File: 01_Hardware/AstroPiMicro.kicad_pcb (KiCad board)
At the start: 2 copper layers, 65 x 50.2 mm, 52 parts, among them J1 RPi Connector, J10 B6B-PH-K(LF)(SN), J2 USB_C_Receptacle_USB2.0, J3 C47647, J4 I2C_IMU, J5 A1002WV-S-4P, J6 B11B-PH-K-S(LF)(SN), J7 B3B-PH-K-S(LF)(SN), J8 CON_SW_B, J9 CON_JOY_B, SW1 SSSS213202, U1 LM809, U2 STM32G431KBTx, U3 MCP73831-2-OT, U4 TPS61090, U5 SKRHAAE010, Y1 X1H016000FI1H-X

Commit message: Finished BOM, PCB and ordered PCB
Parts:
- added G***: LOGO, astropi:qr, B.Cu at (106.5, 63.5)
- D1: value HSMF-C155 -> Status LED
- J10: value B6B-PH-K(LF)(SN) -> 6-pin JST PH
- J3: value C47647 -> 2-pin JST PH
- J4: value I2C_IMU -> 4-pin JST SH
- J5: value A1002WV-S-4P -> 4-pin JST SH
- J6: value B11B-PH-K-S(LF)(SN) -> 11-pin JST PH
- J7: value B3B-PH-K-S(LF)(SN) -> 3-pin JST PH
- J8: value CON_SW_B -> 3-pin JST PH
- J9: value CON_JOY_B -> 6-pin JST PH
- L1: value DR73-6R8-R -> 6.8uH; footprint astropi:DR73 -> Inductor_SMD:L_Taiyo-Yuden_NR-50xx_HandSoldering
- R9: value 2.1Meg -> 2.1M
- SW1: value SSSS213202 -> SW-ON-OFF
- U5: value SKRHAAE010 -> Joystick
- Y1: value X1H016000FI1H-X -> 16MHz
- moved L1 1.11 mm to (64.2, 67.2)
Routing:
- net /GPIO27: track 27.2 -> 26.1 mm, vias 3 -> 2
- net Net-(L1-Pad2): track 6.29 -> 7.15 mm
- net /GPIO17: track 28.7 -> 29.4 mm
- net +3V3: track 61.6 -> 62.1 mm
- net (no net): vias 16 -> 0
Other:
- outline, holes or cut-outs redrawn
- board text added: "[Geanina]"

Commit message: Started on HW version 2
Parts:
- removed the ? at (53.6, 75.5)
- removed the ? at (111.6, 75.6)
- removed G***: LOGO, astropi:qr
- removed J10: 6-pin JST PH, Connector_JST:JST_PH_B6B-PH-K_1x06_P2.00mm_Vertical
- removed J8: 3-pin JST PH, Connector_JST:JST_PH_B3B-PH-SM4-TB_1x03-1MP_P2.00mm_Vertical
- removed J9: 6-pin JST PH, Connector_JST:JST_PH_B6B-PH-SM4-TB_1x06-1MP_P2.00mm_Vertical
- removed REF** (x8): MountingHole_2.2mm_M2_ISO14580_Pad, MountingHole:MountingHole_2.2mm_M2_ISO14580_Pad
- removed Y1: 16MHz, Crystal:Crystal_SMD_Abracon_ABM3B-4Pin_5.0x3.2mm
- added ?: , RPi_Hat:RPi_Hat_Mounting_Hole, F.Cu at (53.6, 101.5)
- added ?: , RPi_Hat:RPi_Hat_Mounting_Hole, F.Cu at (111.6, 101.5)
- added C11: 100nF, Capacitor_SMD:C_0603_1608Metric, F.Cu at (102.7, 73.4)
- added C12: 100nF, Capacitor_SMD:C_0603_1608Metric, F.Cu at (98.2, 62.6)
- added C13: 47uF, Capacitor_Tantalum_SMD:CP_EIA-3528-15_AVX-H, F.Cu at (99.3, 67.4)
- added C14: 100nF, Capacitor_SMD:C_0603_1608Metric, F.Cu at (101.2, 59.5)
- added C15: 100nF, Capacitor_SMD:C_0603_1608Metric, F.Cu at (102.7, 87.1)
- added C16: 100nF, Capacitor_SMD:C_0603_1608Metric, F.Cu at (98.3, 90.4)
- added C17: 47uF, Capacitor_Tantalum_SMD:CP_EIA-3528-15_AVX-H, F.Cu at (99.6, 94.9)
- added C18: 100nF, Capacitor_SMD:C_0603_1608Metric, F.Cu at (101.1, 87.1)
- added C3: 4.7uF, Capacitor_SMD:C_0805_2012Metric, F.Cu at (67.0, 89.7)
- added D2: Orange, LED_SMD:LED_0603_1608Metric, F.Cu at (63.0, 86.2)
- added QR*****: MiniCalinGeani, astropi:MiniCalinGeani, F.Cu at (80.7, 66.9)
- added R11: 0.75, Resistor_SMD:R_0603_1608Metric, F.Cu at (99.0, 73.4)
- added R14: 0.75, Resistor_SMD:R_0603_1608Metric, F.Cu at (103.1, 80.9)
- added R15: 1k, Resistor_SMD:R_0603_1608Metric, F.Cu at (97.8, 59.5)
- added R16: 220m, Resistor_SMD:R_0603_1608Metric, F.Cu at (99.4, 59.5)
- added R17: 220m, Resistor_SMD:R_0603_1608Metric, F.Cu at (102.7, 67.3)
- added R18: 1k, Resistor_SMD:R_0603_1608Metric, F.Cu at (97.7, 87.1)
- added R19: 220m, Resistor_SMD:R_0603_1608Metric, F.Cu at (99.3, 87.1)
- added R20: 220m, Resistor_SMD:R_0603_1608Metric, F.Cu at (103.0, 94.8)
- added R21: 10k, Resistor_SMD:R_0603_1608Metric, F.Cu at (57.8, 91.0)
- added TP1: TP_VBAT, TestPoint:TestPoint_Pad_D2.0mm, F.Cu at (68.9, 75.9)
- added TP2: TP_Supply, TestPoint:TestPoint_Pad_D2.0mm, F.Cu at (73.8, 94.4)
- added TP3: TP_5V, TestPoint:TestPoint_Pad_D2.0mm, F.Cu at (87.2, 81.7)
- added TP4: TP_GND, TestPoint:TestPoint_Pad_2.5x2.5mm, F.Cu at (79.9, 103.2)
- C1: value 27pF -> 100nF; footprint Capacitor_SMD:C_0603_1608Metric_Pad1.05x0.95mm_HandSolder -> Capacitor_SMD:C_0603_1608Metric
- C10: footprint Capacitor_Tantalum_SMD:CP_EIA-7343-31_Kemet-D_Pad2.25x2.55mm_HandSolder -> Capacitor_Tantalum_SMD:CP_EIA-7343-15_Kemet-W
- C2: value 27pF -> 1uF; footprint Capacitor_SMD:C_0603_1608Metric_Pad1.05x0.95mm_HandSolder -> Capacitor_SMD:C_0805_2012Metric
- C4: value 100nF -> 10uF; footprint Capacitor_SMD:C_0603_1608Metric_Pad1.05x0.95mm_HandSolder -> Capacitor_SMD:C_0805_2012Metric
- C5: value 10uF -> 100nF; footprint Capacitor_SMD:C_0805_2012Metric -> Capacitor_SMD:C_0603_1608Metric
- C6: value 100nF -> 47uF; footprint Capacitor_SMD:C_0603_1608Metric_Pad1.05x0.95mm_HandSolder -> Capacitor_Tantalum_SMD:CP_EIA-3528-15_AVX-H
- C7: footprint Capacitor_SMD:C_0603_1608Metric_Pad1.05x0.95mm_HandSolder -> Capacitor_SMD:C_0603_1608Metric
- D1: value Status LED -> Green; footprint LED_SMD:LED_Avago_PLCC4_3.2x2.8mm_CW -> LED_SMD:LED_0603_1608Metric
- J2: value USB_C_Receptacle_USB2.0 -> SHOU_HAN_TYPE-C_6P; footprint astropi:USB_C_GCT_USB4085 -> astropi:SHOU HAN TYPE-C 6P
- J3, J4: moved to F.Cu
- J5: value 4-pin JST SH -> Stepper_Focus; footprint Connector_JST:JST_SH_BM04B-SRSS-TB_1x04-1MP_P1.00mm_Vertical -> Connector_JST:JST_XH_S4B-XH-A_1x04_P2.50mm_Horizontal
- J6: value 11-pin JST PH -> Stepper_Azimuth; footprint Connector_JST:JST_PH_B11B-PH-K_1x11_P2.00mm_Vertical -> Connector_JST:JST_XH_S4B-XH-A_1x04_P2.50mm_Horizontal
- J7: value 3-pin JST PH -> Stepper_Altitude; footprint Connector_JST:JST_PH_B3B-PH-K_1x03_P2.00mm_Vertical -> Connector_JST:JST_XH_S4B-XH-A_1x04_P2.50mm_Horizontal
- L1: value 6.8uH -> 10uH; footprint Inductor_SMD:L_Taiyo-Yuden_NR-50xx_HandSoldering -> astropi:VLS6045EX-100M
- R1: value 10k -> 1.1k; footprint Resistor_SMD:R_0603_1608Metric_Pad1.05x0.95mm_HandSolder -> Resistor_SMD:R_0603_1608Metric
- R10, R12, R13, R4, R5, R7, R8, R9: footprint Resistor_SMD:R_0603_1608Metric_Pad1.05x0.95mm_HandSolder -> Resistor_SMD:R_0603_1608Metric
- R2: value 10k -> 1k; footprint Resistor_SMD:R_0603_1608Metric_Pad1.05x0.95mm_HandSolder -> Resistor_SMD:R_0603_1608Metric
- R3: value 10k -> 1.5k; footprint Resistor_SMD:R_0603_1608Metric_Pad1.05x0.95mm_HandSolder -> Resistor_SMD:R_0603_1608Metric
- R6: value 2k -> 10k; footprint Resistor_SMD:R_0603_1608Metric_Pad1.05x0.95mm_HandSolder -> Resistor_SMD:R_0603_1608Metric
- SW1: value SW-ON-OFF -> SW_SPDT; footprint astropi:SSSS213202 -> Button_Switch_SMD:SW_SPDT_CK-JS102011SAQN
- U1: value LM809 -> BQ24074RGT; footprint Package_TO_SOT_SMD:SOT-23 -> Package_DFN_QFN:VQFN-16-1EP_3x3mm_P0.5mm_EP1.6x1.6mm_ThermalVias
- U2: value STM32G431KBTx -> TMC2300; footprint Package_QFP:LQFP-32_7x7mm_P0.8mm -> Package_DFN_QFN:QFN-20-1EP_3x3mm_P0.4mm_EP1.65x1.65mm_ThermalVias
- U3: value MCP73831-2-OT -> TMC2300; footprint Package_TO_SOT_SMD:SOT-23-5 -> Package_DFN_QFN:QFN-20-1EP_3x3mm_P0.4mm_EP1.65x1.65mm_ThermalVias
- U5: value Joystick -> TMC2300; footprint astropi:SKRHAAE010 -> Package_DFN_QFN:QFN-20-1EP_3x3mm_P0.4mm_EP1.65x1.65mm_ThermalVias
- moved R1 55.0 mm to (60.9, 93.3), turned to 90 degrees
- moved U1 52.7 mm to (63.9, 90.8), turned to 180 degrees
- moved C2 52.1 mm to (63.6, 94.0)
- moved C4 43.9 mm to (60.7, 89.8), turned to 90 degrees
- moved C5 43.2 mm to (98.2, 76.5)
- moved SW1 39.4 mm to (52.3, 91.6), turned to 270 degrees
- moved J2 38.1 mm to (64.0, 99.6), turned to 0 degrees
- moved J7 36.8 mm to (107.0, 94.6), turned to 90 degrees
- moved R3 36.1 mm to (66.8, 93.3), turned to 90 degrees
- moved U3 34.8 mm to (101.3, 63.2), turned to 90 degrees
- moved R4 33.7 mm to (63.1, 96.7), turned to 270 degrees
- moved U5 32.9 mm to (101.3, 90.8), turned to 90 degrees
- moved R5 32.3 mm to (64.7, 96.7), turned to 270 degrees
- moved R6 31.3 mm to (68.9, 93.2), turned to 270 degrees
- moved R8 29.6 mm to (68.1, 86.2), turned to 90 degrees
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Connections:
- C1 pad 1: Net-(C1-Pad1) -> +3V3
- C2 pad 1: Net-(C2-Pad1) -> VBUS
- C4 pad 1: +3V3 -> /Vsupply
- C5 pad 1: VBUS -> +5V
- C6 pad 1: +3V3 -> +5V
- C7 pad 1: +3V3 -> Net-(C7-Pad1)
- C8 pad 1: +BATT -> /Vsupply
- D1 pad 2: VBUS -> Net-(D1-Pad2)
- J1 pad 10: /PI_UART_RX -> /UART_RX
- J1 pad 11: /GPIO17 -> /STEP_Focus
- J1 pad 13: /GPIO27 -> /DIR_Focus
- J1 pad 15: /GPIO22 -> /ERR_Focus
- J1 pad 16: /GPIO23 -> (no net)
- J1 pad 18: Net-(J1-Pad18) -> (no net)
- J1 pad 19: /LCD_MOSI -> /STEP_Az
- J1 pad 21: /LCD_TDC -> /DIR_Az
- J1 pad 22: Net-(J1-Pad22) -> (no net)
- J1 pad 23: /LCD_SCK -> /ERR_Az
- J1 pad 24: Net-(J1-Pad24) -> (no net)
- J1 pad 26: /LCD_~TCS -> (no net)
- J1 pad 27: Net-(J1-Pad27) -> (no net)
- J1 pad 28: Net-(J1-Pad28) -> (no net)
- J1 pad 29: Net-(J1-Pad29) -> /STEP_Alt
- J1 pad 3: Net-(J1-Pad3) -> /IMU_SDA
- J1 pad 31: Net-(J1-Pad31) -> /DIR_Alt
- J1 pad 32: Net-(J1-Pad32) -> (no net)
- J1 pad 33: Net-(J1-Pad33) -> /ERR_Alt
- J1 pad 35: /LCD_BL -> (no net)
- J1 pad 36: Net-(J1-Pad36) -> (no net)
- J1 pad 37: Net-(J1-Pad37) -> (no net)
- J1 pad 38: Net-(J1-Pad38) -> (no net)
- J1 pad 40: Net-(J1-Pad40) -> (no net)
- J1 pad 5: Net-(J1-Pad5) -> /IMU_SCL
- J1 pad 7: /GPIO4 -> (no net)
- J1 pad 8: /PI_UART_TX -> /UART_TX
- J5 pad 1: +3V3 -> /Focus_A1
- J5 pad 2: /SWDIO -> /Focus_A2
- J5 pad 3: /SWCLK -> /Focus_B1
- J5 pad 4: GND -> /Focus_B2
- J6 pad 1: +5V -> /Az_A1
- J6 pad 2: /LCD_3V3 -> /Az_A2
- J6 pad 3: GND -> /Az_B1
- J6 pad 4: /LCD_SCK -> /Az_B2
- J7 pad 1: +BATT -> /Alt_A1
- J7 pad 2: /ON\~OFF -> /Alt_A2
- J7 pad 3: GND -> /Alt_B1
- L1 pad 1: +BATT -> /Vsupply
- R1 pad 1: +3V3 -> GND
- R1 pad 2: /~RESET -> Net-(R1-Pad2)
- R2 pad 1: Net-(R2-Pad1) -> /UART_TX
- R2 pad 2: GND -> /UART_RX
- R3 pad 1: +3V3 -> GND
- R3 pad 2: Net-(R2-Pad1) -> Net-(R3-Pad2)
- R7 pad 1: Net-(D1-Pad1) -> /Vsupply
- R7 pad 2: /CHG_ST -> Net-(D1-Pad2)
- R8 pad 1: Net-(D1-Pad3) -> /Vsupply
- R8 pad 2: GND -> Net-(D2-Pad2)
- R9 pad 1: +BATT -> /Vsupply
- SW1 pad 1: /SW_1 -> GND
- SW1 pad 2: /SW_2 -> /ON\~OFF
- SW1 pad 3: /SW_3 -> (no net)
- U1 pad 1: GND -> Net-(R6-Pad1)
- U1 pad 2: /~RESET -> +BATT
- U1 pad 3: +3V3 -> +BATT
- U2 pad 1: +3V3 -> /Focus_A2
- U2 pad 10: Net-(U2-Pad10) -> /UART_RX
- U2 pad 11: Net-(U2-Pad11) -> +3V3
- U2 pad 12: Net-(U2-Pad12) -> /ERR_Focus
- U2 pad 13: Net-(U2-Pad13) -> Net-(C7-Pad1)
- U2 pad 15: +3V3 -> /Focus_B2
- U2 pad 16: GND -> Net-(R11-Pad1)
- U2 pad 17: +3V3 -> /Focus_B1
- U2 pad 18: /IMU_SDA -> +5V
- U2 pad 19: /IMU_SCL -> /Focus_A1
- U2 pad 2: Net-(C1-Pad1) -> (no net)
- U2 pad 21: Net-(U2-Pad21) -> GND
- U2 pad 3: Net-(C2-Pad1) -> /DIR_Focus
- U2 pad 4: /~RESET -> /STEP_Focus
- U2 pad 5: Net-(U2-Pad5) -> GND
- U2 pad 6: Net-(U2-Pad6) -> GND
- U2 pad 7: /PI_UART_RX -> +3V3
- U2 pad 8: /PI_UART_TX -> +3V3
- U2 pad 9: Net-(U2-Pad9) -> GND
- U3 pad 1: /CHG_ST -> /Az_A2
- U3 pad 2: GND -> (no net)
- U3 pad 3: +BATT -> /DIR_Az
- U3 pad 4: VBUS -> /STEP_Az
- U3 pad 5: Net-(R6-Pad1) -> +3V3
- U4 pad 2: Net-(U4-Pad2) -> (no net)
- U4 pad 8: +BATT -> /Vsupply
- U5 pad 1: /JOY_A -> /Alt_A2
- U5 pad 2: /JOY_PUSH -> (no net)
- U5 pad 3: /JOY_C -> /DIR_Alt
- U5 pad 4: /JOY_B -> /STEP_Alt
- U5 pad 5: /JOY_GND -> +3V3
- U5 pad 6: /JOY_D -> +3V3
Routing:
- net /UART_RX: track 0.00 -> 129.2 mm, vias 0 -> 6
- net /DIR_Alt: track 0.00 -> 73.1 mm
- net /UART_TX: track 0.00 -> 71.2 mm, vias 0 -> 4
- net +3V3: track 62.1 -> 130.2 mm, vias 6 -> 4
- net /STEP_Alt: track 0.00 -> 65.8 mm
- net /ERR_Alt: track 0.00 -> 54.5 mm, vias 0 -> 1
- net /Vsupply: track 0.00 -> 53.3 mm, vias 0 -> 2
- net /STEP_Focus: track 0.00 -> 47.6 mm
- net /DIR_Focus: track 0.00 -> 45.4 mm
- net /PI_UART_RX: track 42.2 -> 0.00 mm, vias 2 -> 0
- net /GPIO4: track 41.3 -> 0.00 mm, vias 4 -> 0
- net /PI_UART_TX: track 39.6 -> 0.00 mm, vias 2 -> 0
- net /IMU_SCL: track 53.7 -> 14.8 mm, vias 5 -> 0
- net /IMU_SDA: track 51.0 -> 12.8 mm, vias 3 -> 0
- net /ERR_Focus: track 0.00 -> 36.8 mm
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- added copper zone on In1, net +5V
- added copper zone on In2, net GND
- removed copper zone on F.Cu, net +3V3
- removed copper zone on F.Cu, net +5V
- removed copper zone on B.Cu, net GND
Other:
- board size 65 x 50.2 mm -> 65.1 x 56 mm
- copper layers 2 -> 4
- board text removed: "<NP"

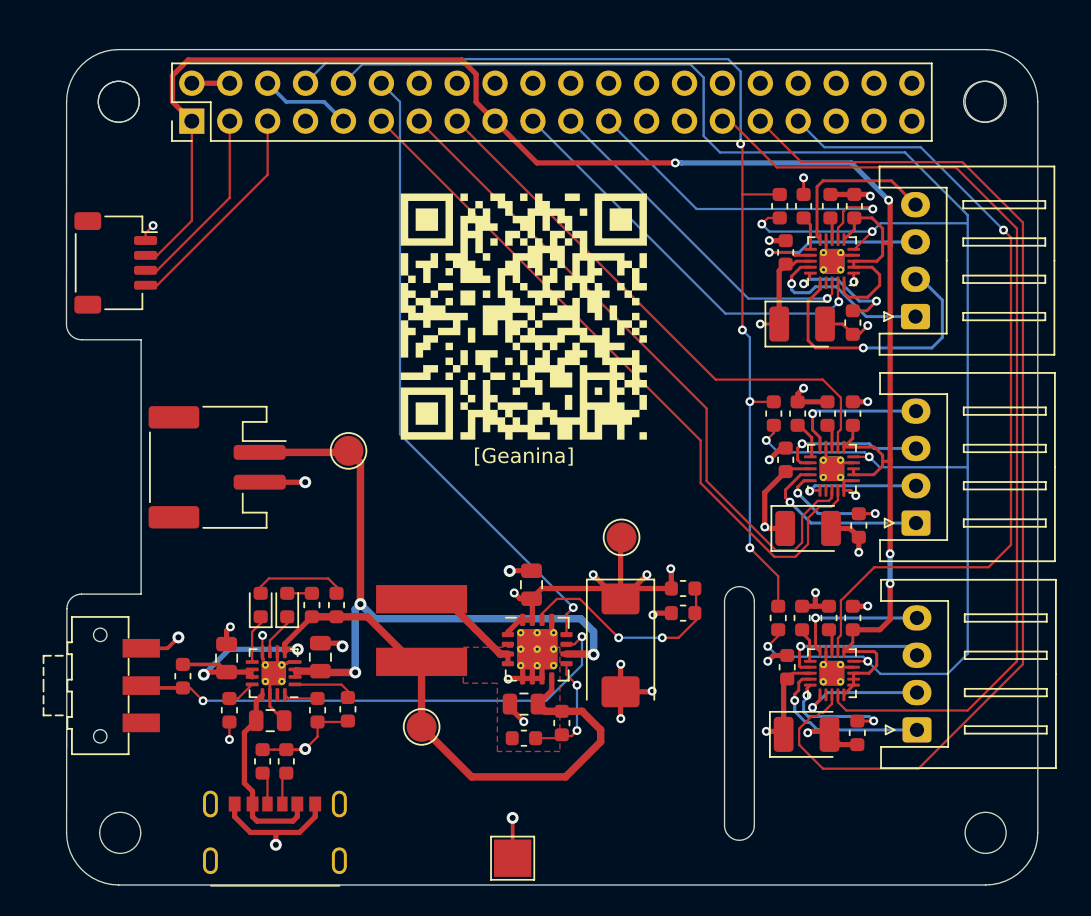
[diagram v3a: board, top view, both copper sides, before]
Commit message: Ordered PCBs from JLCPCB
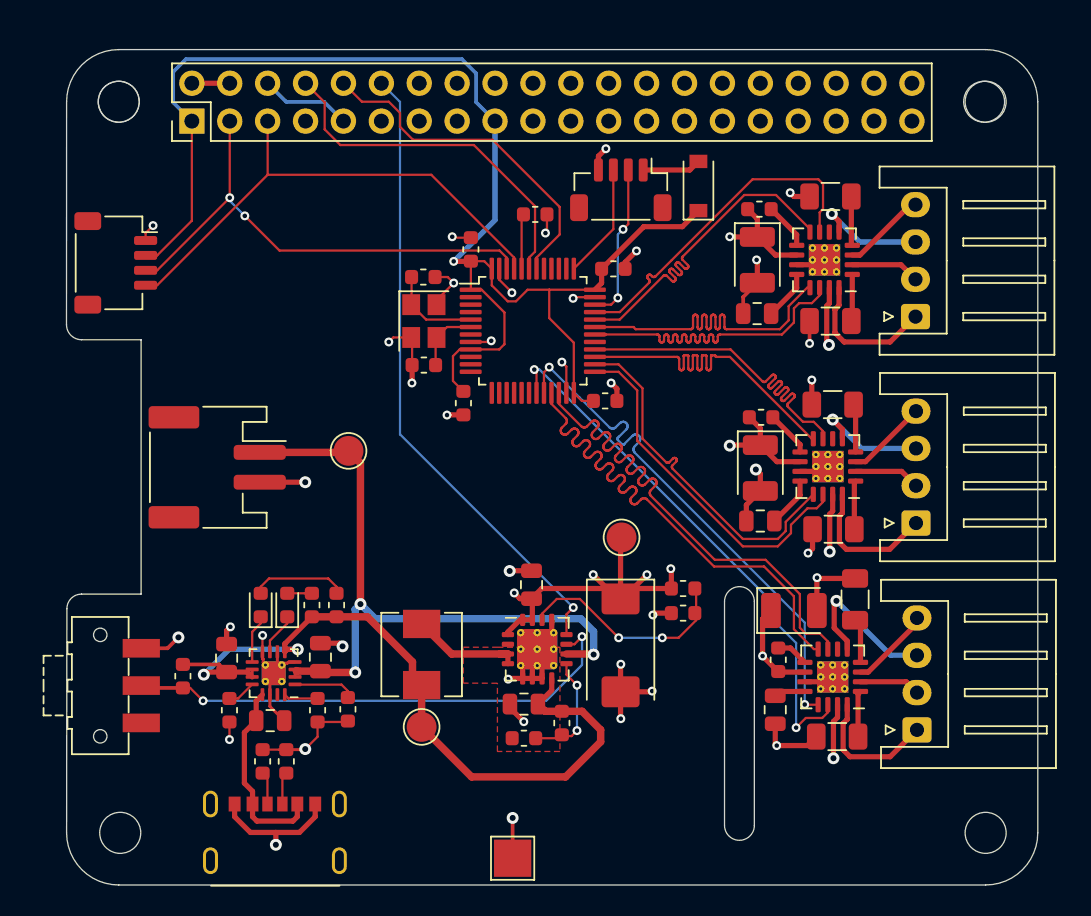
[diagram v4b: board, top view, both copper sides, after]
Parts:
- removed R15, R18: 1k, Resistor_SMD:R_0603_1608Metric
- added C19: 100nF, Capacitor_SMD:C_0603_1608Metric, F.Cu at (76.6, 72.7)
- added C20: 100nF, Capacitor_SMD:C_0603_1608Metric, F.Cu at (77.1, 62.4)
- added C21: 100nF, Capacitor_SMD:C_0603_1608Metric, F.Cu at (86.1, 72.5)
- added D3: B5819W, Diode_SMD:D_SOD-123, F.Cu at (92.3, 58.1)
- added J8: SWD, Connector_JST:JST_SH_BM04B-SRSS-TB_1x04-1MP_P1.00mm_Vertical, F.Cu at (87.2, 58.4)
- added U6: DRV8833RTY, Package_DFN_QFN:Texas_S-PWQFN-N16_EP2.1x2.1mm_ThermalVias, F.Cu at (100.8, 63.1)
- added Y1: 16MHz, Crystal:Crystal_SMD_3225-4Pin_3.2x2.5mm, F.Cu at (74.0, 67.2)
- C1, C5: value 100nF -> 20pF
- C11, C14, C16: value 100nF -> 10nF
- C12, C15, C18: value 100nF -> 2.2uF; footprint Capacitor_SMD:C_0603_1608Metric -> Capacitor_SMD:C_0805_2012Metric
- L1: footprint astropi:VLS6045EX-100M -> Inductor_SMD:L_Sunlord_MWSA0518_5.4x5.2mm
- QR*****: moved to B.Cu
- R11, R14: value 0.75 -> 1; footprint Resistor_SMD:R_0603_1608Metric -> Resistor_SMD:R_1206_3216Metric
- R12: value 1.85Meg -> 2M
- R13: value 200k -> 220k
- R16, R17, R19, R20: footprint Resistor_SMD:R_0603_1608Metric -> Resistor_SMD:R_1206_3216Metric
- R2: value 1k -> 10k
- R9: value 2.1M -> 2M
- U2: value TMC2300 -> STM32F103C8Tx; footprint Package_DFN_QFN:QFN-20-1EP_3x3mm_P0.4mm_EP1.65x1.65mm_ThermalVias -> Package_QFP:LQFP-48_7x7mm_P0.5mm
- U3, U5: value TMC2300 -> DRV8833RTY; footprint Package_DFN_QFN:QFN-20-1EP_3x3mm_P0.4mm_EP1.65x1.65mm_ThermalVias -> Package_DFN_QFN:Texas_S-PWQFN-N16_EP2.1x2.1mm_ThermalVias
- U4: value TPS61090 -> TPS61030
- moved R16 35.6 mm to (101.7, 95.0), turned to 180 degrees
- moved C17 32.0 mm to (96.3, 63.1), turned to 270 degrees
- moved C16 30.8 mm to (96.4, 59.7), turned to 0 degrees
- moved C14 30.6 mm to (97.7, 89.9)
- moved C1 29.3 mm to (73.9, 64.2), turned to 0 degrees
- moved R19 28.3 mm to (101.2, 58.9), turned to 180 degrees
- moved R20 27.7 mm to (101.2, 67.2), turned to 180 degrees
- moved C5 25.1 mm to (74.0, 70.2), turned to 180 degrees
- moved U2 22.1 mm to (81.2, 67.8), turned to 0 degrees
- moved C18 21.0 mm to (96.3, 66.7), turned to 180 degrees
- moved R2 20.8 mm to (81.4, 60.0), turned to 0 degrees
- moved C13 19.2 mm to (98.8, 86.6)
- moved R17 18.6 mm to (102.8, 85.8), turned to 90 degrees
- moved C12 18.1 mm to (96.5, 80.6), turned to 180 degrees
- moved C7 17.3 mm to (86.7, 63.7), turned to 0 degrees
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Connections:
- C1 pad 1: +3V3 -> Net-(C1-Pad1)
- C11 pad 1: +3V3 -> +5V
- C11 pad 2: GND -> Net-(C11-Pad2)
- C12 pad 1: +5V -> Net-(C12-Pad1)
- C14 pad 1: Net-(C14-Pad1) -> +5V
- C14 pad 2: GND -> Net-(C14-Pad2)
- C15 pad 1: +3V3 -> Net-(C15-Pad1)
- C16 pad 2: GND -> Net-(C16-Pad2)
- C5 pad 1: +5V -> Net-(C5-Pad1)
- C7 pad 1: Net-(C7-Pad1) -> +3V3
- J1 pad 11: /STEP_Focus -> (no net)
- J1 pad 13: /DIR_Focus -> (no net)
- J1 pad 15: /ERR_Focus -> (no net)
- J1 pad 19: /STEP_Az -> (no net)
- J1 pad 21: /DIR_Az -> (no net)
- J1 pad 23: /ERR_Az -> (no net)
- J1 pad 29: /STEP_Alt -> (no net)
- J1 pad 31: /DIR_Alt -> (no net)
- J1 pad 33: /ERR_Alt -> (no net)
- R2 pad 1: /UART_TX -> Net-(R2-Pad1)
- R2 pad 2: /UART_RX -> GND
- U2 pad 1: /Focus_A2 -> +3V3
- U2 pad 10: /UART_RX -> (no net)
- U2 pad 11: +3V3 -> (no net)
- U2 pad 12: /ERR_Focus -> (no net)
- U2 pad 13: Net-(C7-Pad1) -> (no net)
- U2 pad 14: GND -> (no net)
- U2 pad 15: /Focus_B2 -> (no net)
- U2 pad 16: Net-(R11-Pad1) -> (no net)
- U2 pad 17: /Focus_B1 -> (no net)
- U2 pad 18: +5V -> (no net)
- U2 pad 19: /Focus_A1 -> /A1_ALT
- U2 pad 20: Net-(R14-Pad1) -> /A2_ALT
- U2 pad 21: GND -> /B2_ALT
- U2 pad 3: /DIR_Focus -> (no net)
- U2 pad 4: /STEP_Focus -> (no net)
- U2 pad 5: GND -> Net-(C1-Pad1)
- U2 pad 6: GND -> Net-(C5-Pad1)
- U2 pad 7: +3V3 -> (no net)
- U2 pad 8: +3V3 -> GND
- U2 pad 9: GND -> +3V3
- U3 pad 1: /Az_A2 -> Net-(R11-Pad1)
- U3 pad 10: /UART_RX -> +5V
- U3 pad 11: +3V3 -> GND
- U3 pad 12: /ERR_Az -> Net-(C12-Pad1)
- U3 pad 13: Net-(C14-Pad1) -> /A2_FOCUS
- U3 pad 14: GND -> /A1_FOCUS
- U3 pad 15: /Az_B2 -> +5V
- U3 pad 16: Net-(R16-Pad1) -> /Focus_A1
- U3 pad 17: /Az_B1 -> GND
- U3 pad 2: (no net) -> /Focus_A2
- U3 pad 3: /DIR_Az -> /Focus_B2
- U3 pad 4: /STEP_Az -> Net-(R14-Pad1)
- U3 pad 5: +3V3 -> /Focus_B1
- U3 pad 6: GND -> (no net)
- U3 pad 7: +3V3 -> /B1_FOCUS
- U3 pad 8: +3V3 -> /B2_FOCUS
- U3 pad 9: GND -> Net-(C11-Pad2)
- U5 pad 1: /Alt_A2 -> Net-(R16-Pad1)
- U5 pad 10: /UART_RX -> +5V
- U5 pad 11: +3V3 -> GND
- U5 pad 12: /ERR_Alt -> Net-(C15-Pad1)
- U5 pad 13: Net-(C18-Pad1) -> /A2_ALT
- U5 pad 14: GND -> /A1_ALT
- U5 pad 15: /Alt_B2 -> +5V
- U5 pad 16: Net-(R19-Pad1) -> /Alt_A1
- U5 pad 17: /Alt_B1 -> GND
- U5 pad 2: (no net) -> /Alt_A2
- U5 pad 3: /DIR_Alt -> /Alt_B2
- U5 pad 4: /STEP_Alt -> Net-(R17-Pad1)
- U5 pad 5: +3V3 -> /Alt_B1
- U5 pad 6: +3V3 -> (no net)
- U5 pad 7: +3V3 -> /B1_ALT
- U5 pad 8: +3V3 -> /B2_ALT
- U5 pad 9: GND -> Net-(C14-Pad2)
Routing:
- net /UART_RX: track 129.2 -> 23.2 mm, vias 6 -> 0
- net /DIR_Alt: track 73.1 -> 0.00 mm
- net /STEP_Alt: track 65.8 -> 0.00 mm
- net /ERR_Alt: track 54.5 -> 0.00 mm, vias 1 -> 0
- net /STEP_Focus: track 47.6 -> 0.00 mm
- net /UART_TX: track 71.2 -> 24.2 mm, vias 4 -> 0
- net /DIR_Focus: track 45.4 -> 0.00 mm
- net /ERR_Focus: track 36.8 -> 0.00 mm
- net +3V3: track 130.2 -> 93.6 mm, vias 4 -> 1
- net /A1_ALT: track 0.00 -> 36.2 mm, vias 0 -> 2
- net /B2_ALT: track 0.00 -> 36.1 mm
- net /B1_ALT: track 0.00 -> 36.1 mm
- net /A2_ALT: track 0.00 -> 36.0 mm, vias 0 -> 2
- net /STEP_Az: track 27.5 -> 0.00 mm, vias 1 -> 0
- net /ERR_Az: track 24.3 -> 0.00 mm, vias 1 -> 0
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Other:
- net class HighPower added: clearance 0.2, trace_width 0.35, via_dia 0.8, via_drill 0.4

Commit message: Changed layers to Sig, GND, PWR, Sig
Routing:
- added copper zone on In2, net +5V
- added copper zone on In1, net GND
- removed copper zone on In1, net +5V
- removed copper zone on In2, net GND
